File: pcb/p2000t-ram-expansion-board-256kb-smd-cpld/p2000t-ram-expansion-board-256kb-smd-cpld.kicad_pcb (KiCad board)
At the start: 2 copper layers, 75.4 x 45.5 mm, 16 parts, among them J1 EXPANSION BOARD, J2 POWER, J3 TERMINAL, J4 Atmel-JTAG-10, U1 ATF1502ASV, U2 62128, U3 62128

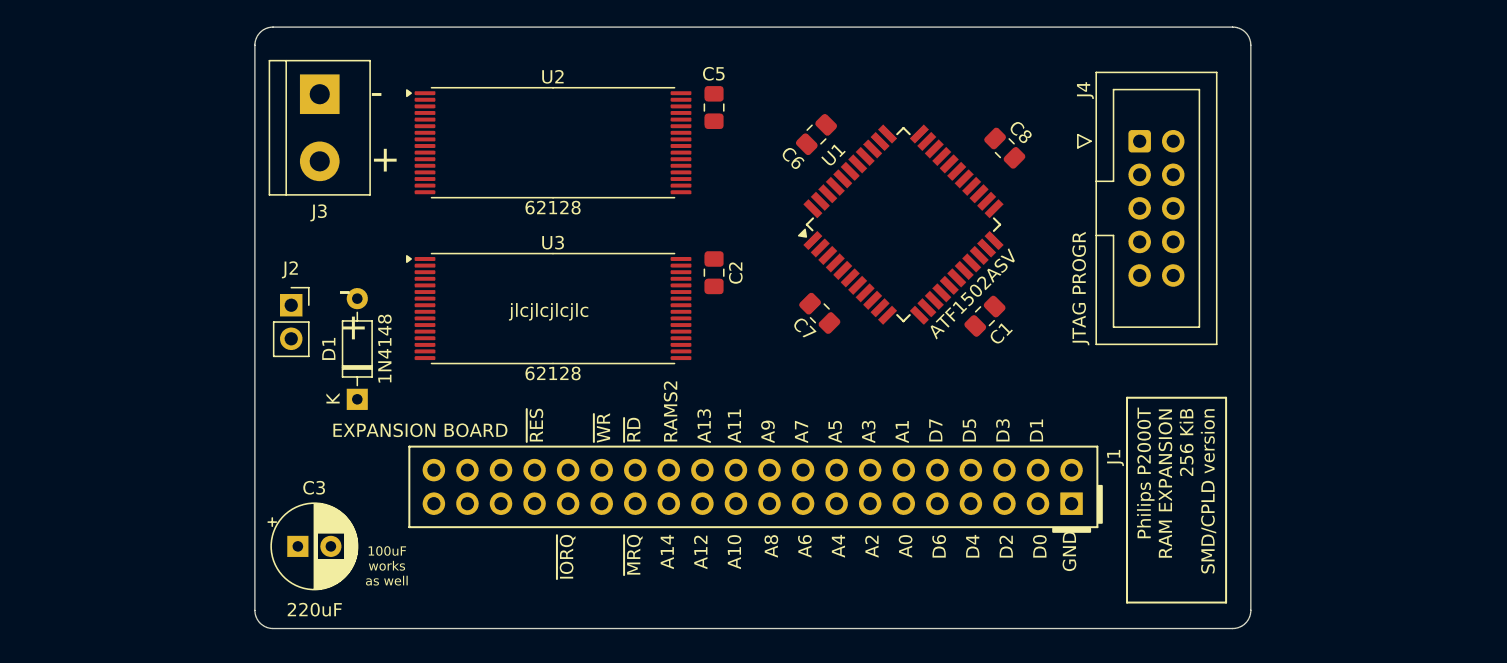
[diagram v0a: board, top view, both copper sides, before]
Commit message: Expanding to 4 RAM chips
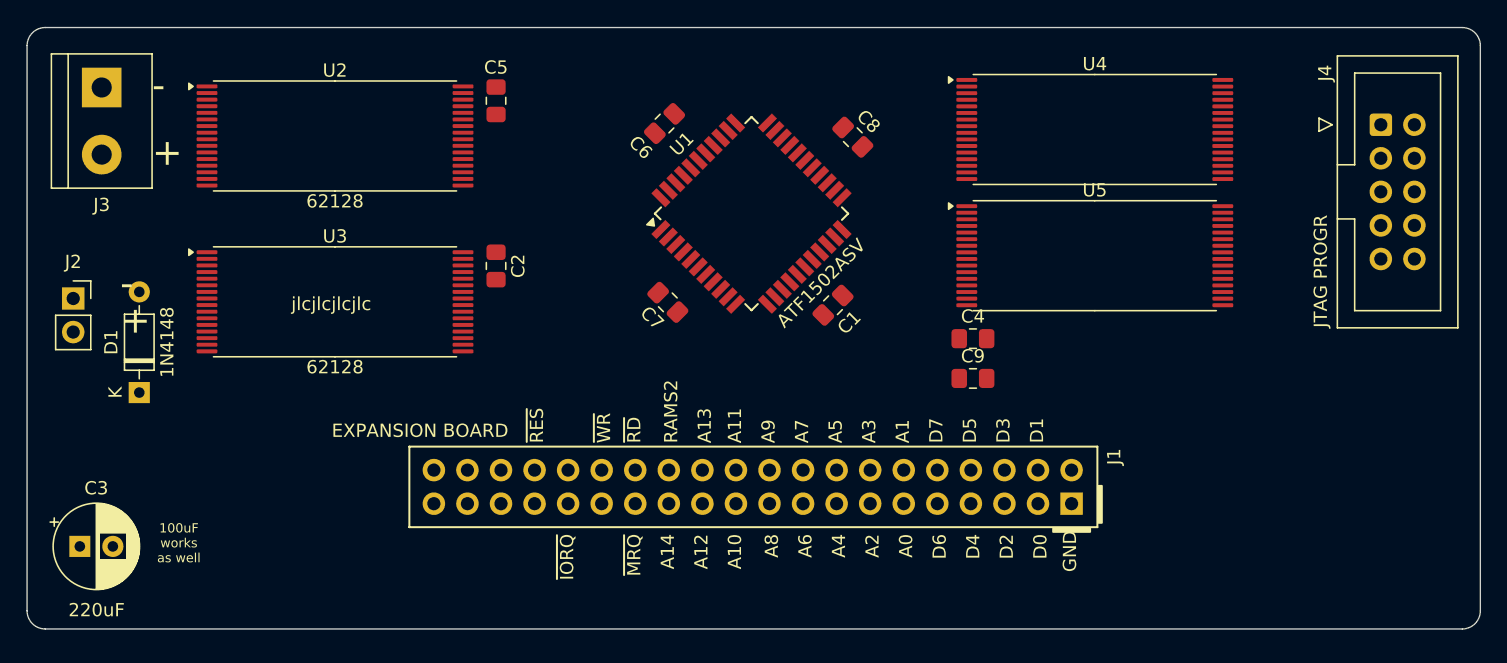
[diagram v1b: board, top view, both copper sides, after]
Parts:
- added C4: 0.1uF, Capacitor_SMD:C_0805_2012Metric_Pad1.18x1.45mm_HandSolder, F.Cu at (91.6, 68.0)
- added C9: 0.1uF, Capacitor_SMD:C_0805_2012Metric_Pad1.18x1.45mm_HandSolder, F.Cu at (91.6, 71.0)
- added U4: 62128, Package_SO:TSOP-I-32_18.4x8mm_P0.5mm, F.Cu at (100.8, 52.2)
- added U5: 62128, Package_SO:TSOP-I-32_18.4x8mm_P0.5mm, F.Cu at (100.8, 61.8)
- moved J4 18.3 mm to (122.5, 51.8)
- moved C2 16.5 mm to (55.5, 62.5)
- moved C5 16.5 mm to (55.5, 50.0)
- moved D1 16.5 mm to (28.5, 72.1)
- moved G*** 16.5 mm to (45.0, 54.2)
- moved J2 16.5 mm to (23.5, 65.0)
- moved J3 16.5 mm to (25.7, 49.0)
- moved U2 16.5 mm to (43.3, 52.7)
- moved U3 16.5 mm to (43.3, 65.2)
- moved C3 16.5 mm to (24.0, 83.8)
- moved C1 11.5 mm to (81.0, 65.5)
- moved C6 11.5 mm to (68.2, 51.8)
- moved C8 11.5 mm to (82.5, 52.8)
- moved U1 11.5 mm to (74.8, 58.6)
- moved C7 11.5 mm to (68.5, 65.3)
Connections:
- U1 pad 14: ~{MRQ} -> ~{CS4}
- U1 pad 39: unconnected-(U1-I/GCLR-Pad39) -> ~{RES}
- U1 pad 40: ~{RES} -> ~{MRQ}
- U1 pad 5: unconnected-(U1-I/O/PD1-Pad5) -> ~{CS3}
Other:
- board size 75.4 x 45.5 mm -> 110 x 45.5 mm
- board text removed: "Philips P2000T RAM EXPANSION 256 KiB SMD/CPLD version"
